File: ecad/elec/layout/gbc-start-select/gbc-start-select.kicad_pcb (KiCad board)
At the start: 2 copper layers, 225.7 x 100.8 mm, 0 parts

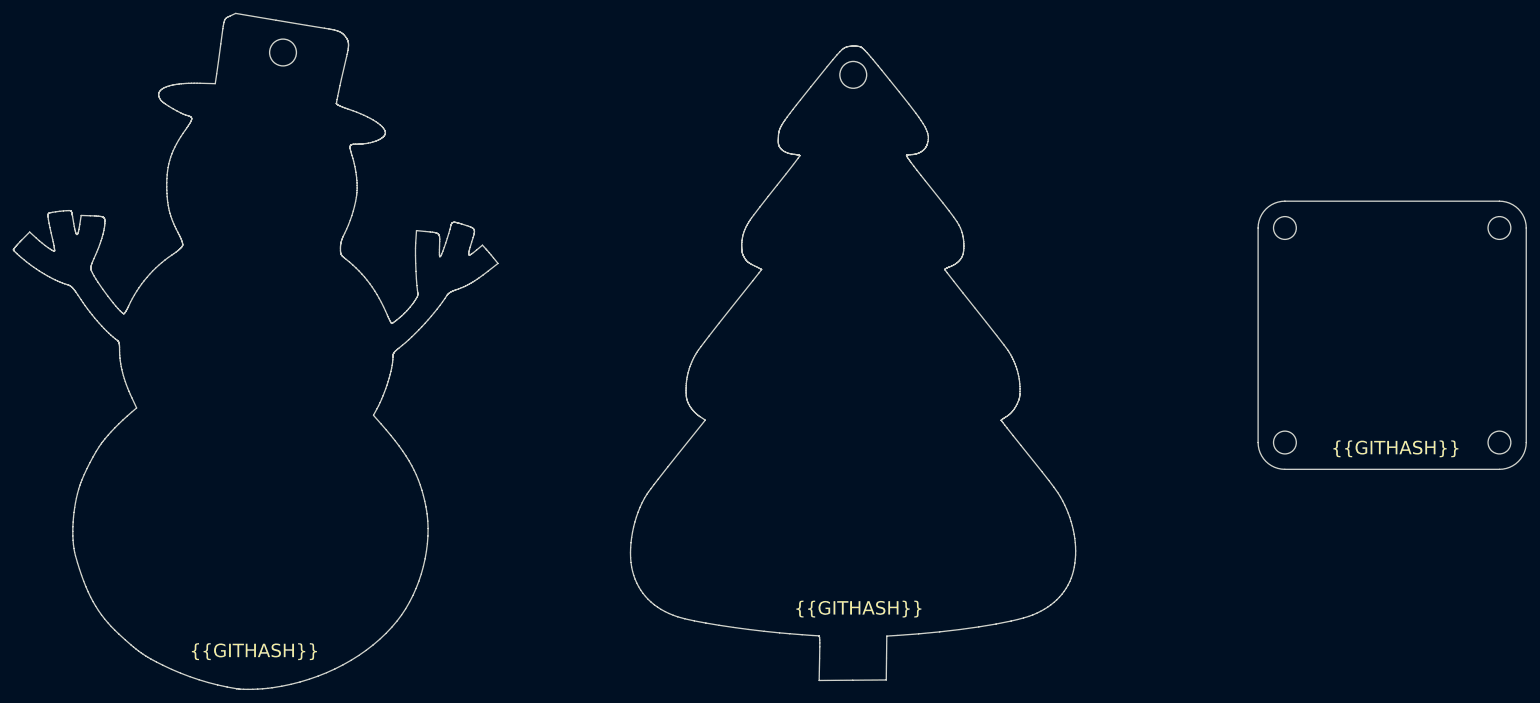
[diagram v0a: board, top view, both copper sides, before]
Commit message: WIP fleshing out and redoing some of the design to add some footprints / components for slik / membranes / etc.
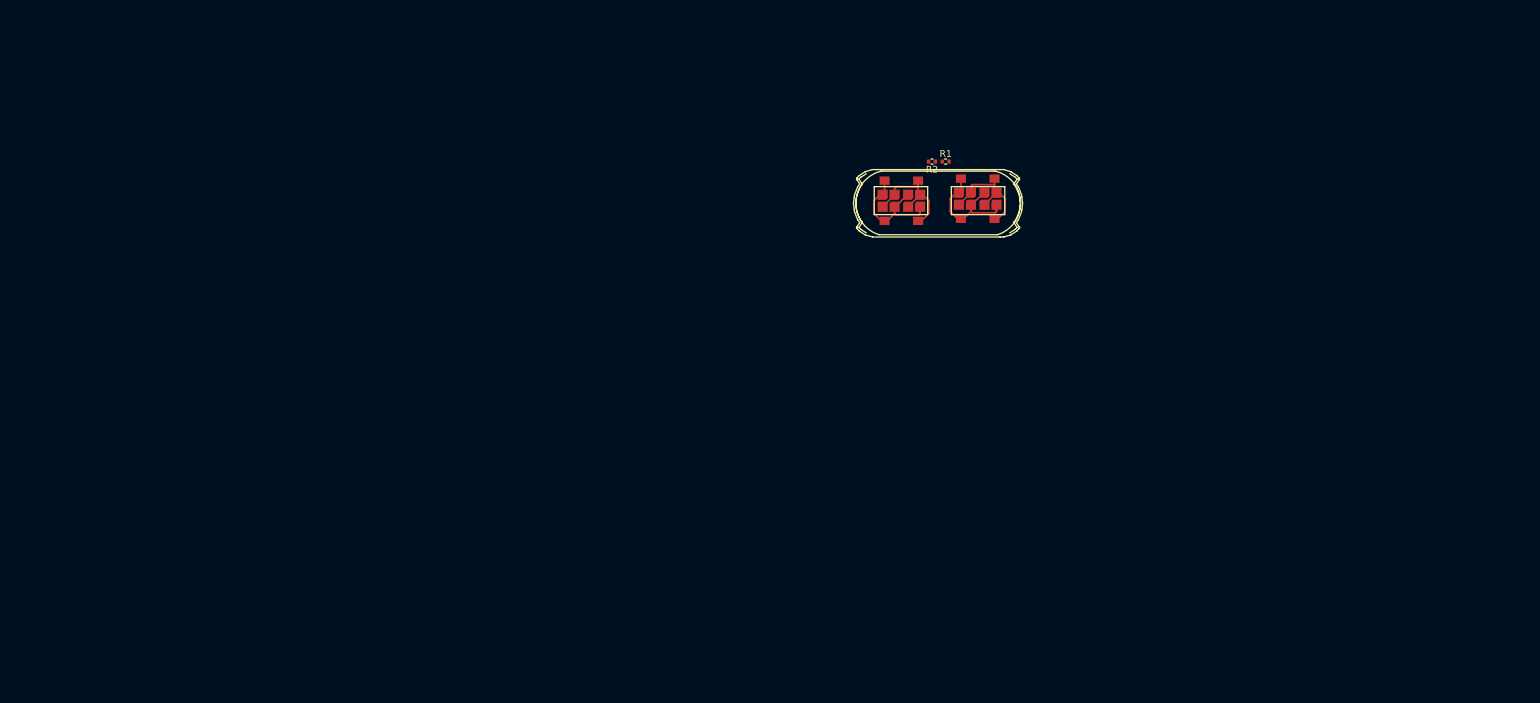
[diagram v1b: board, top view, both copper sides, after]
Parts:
- added R1: 62.5mW Thick Film Resistors 50V ±100ppm/℃ ±1% 10kΩ 0402 Chi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, lib:R0402, F.Cu at (175.0, 71.9)
- added R2: 62.5mW Thick Film Resistors 50V ±100ppm/℃ ±1% 10kΩ 0402 Chi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, lib:R0402, F.Cu at (173.0, 71.9)
- added U1: , lib:GAMEBOY_COLOR_START_SELECT_MEMBRANE, F.Cu at (173.6, 77.7)
- added U2: , lib:GBC_START_SELECT_BUTTON, F.Cu at (179.8, 77.4)
- added U3: , lib:GBC_START_SELECT_BUTTON, F.Cu at (168.4, 77.7)
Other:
- board outline removed
- board text removed: "{{GITHASH}}"
